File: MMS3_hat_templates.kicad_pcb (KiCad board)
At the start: 4 copper layers, 100 x 50 mm, 62 parts, among them J1 Chainbus in, J2 Chainbus Out, J3 Conn_01x04_Pin, J4 AMASS XT60 Male, J5 AMASS XT60 Female, J8 Conn_01x03_Pin, SW1 SW_DIP_x04, U2 M24C64, U3 SN74CB3Q3245PWR, U4 AMS1117, U5 LM2596HVS-ADJRG

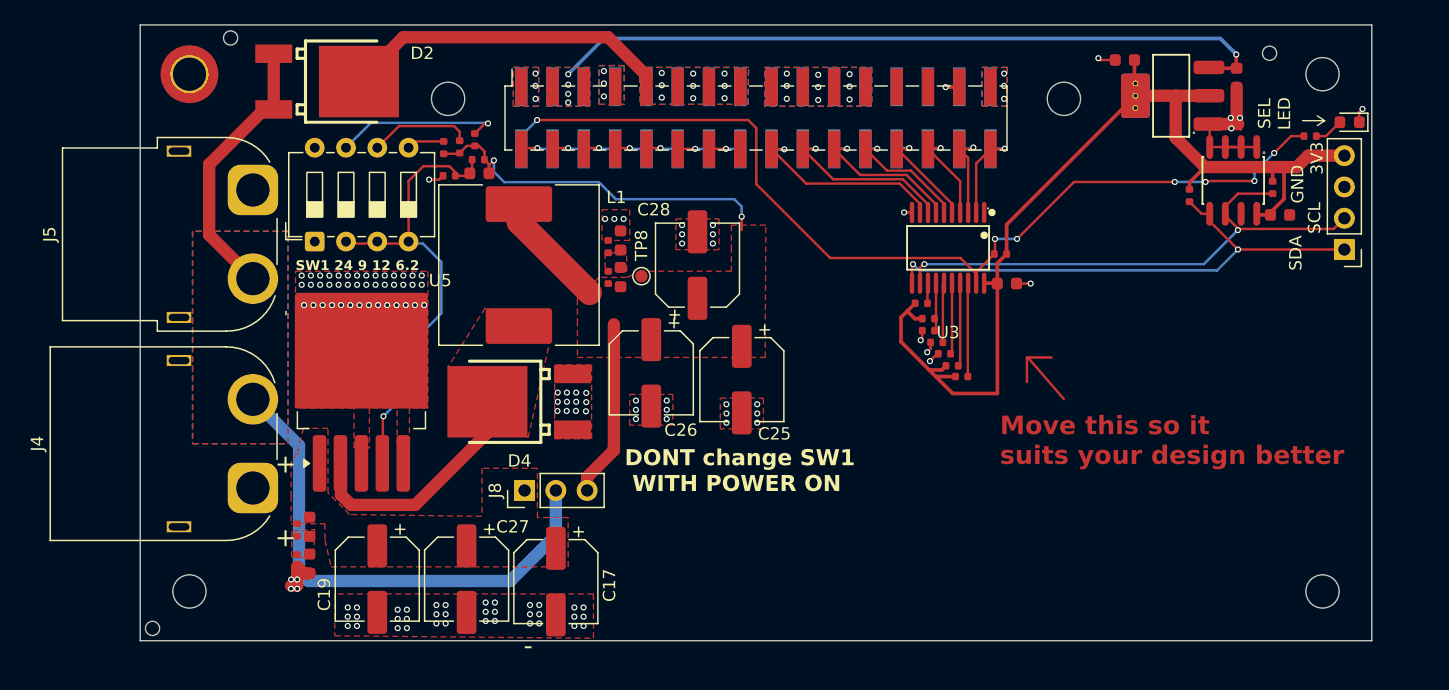
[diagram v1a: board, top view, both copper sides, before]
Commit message: added rounded corners
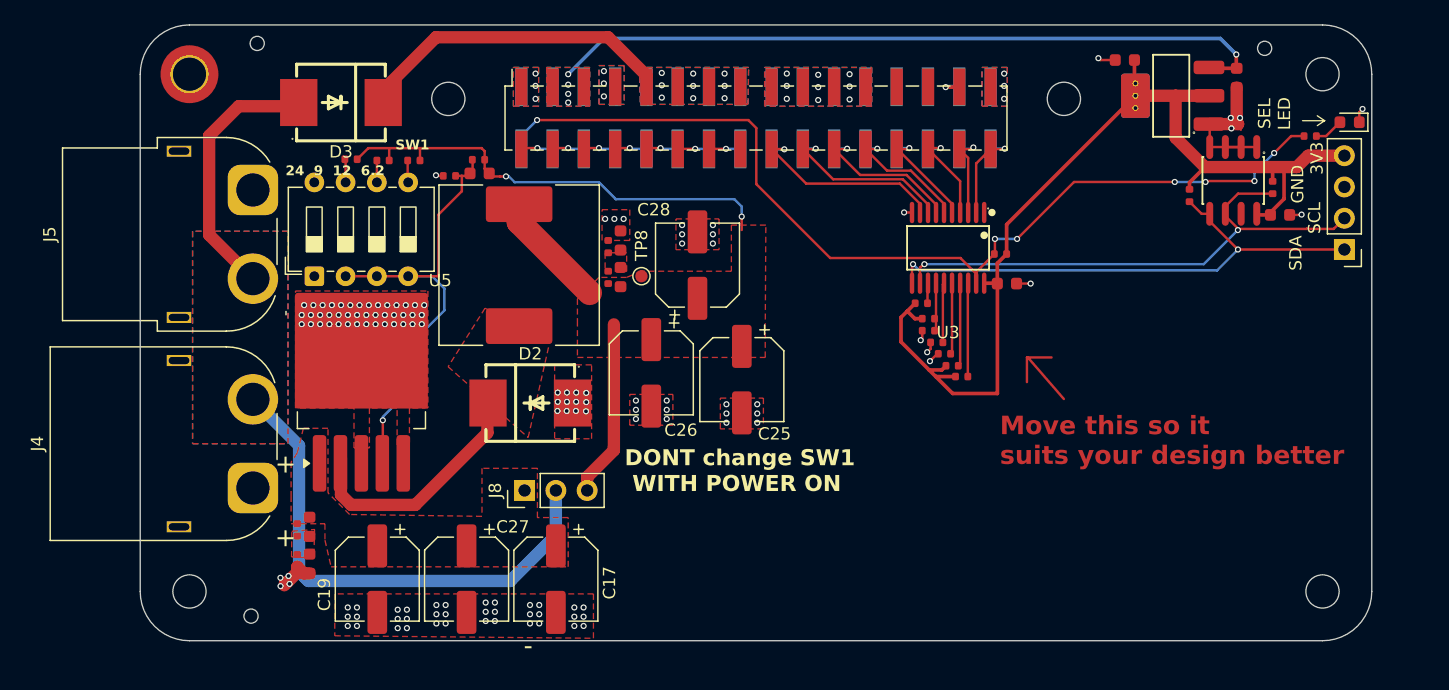
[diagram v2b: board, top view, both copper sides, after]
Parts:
- removed D4: MBRD10100CTTR, SMC_MBRD10100CTTR:TO-252-3_L6.5-W5.8-P4.58-TL
- removed PN1: ~, PCM_JLCPCB:Part_Num_JLCPCB
- added D3: SS510C, SS510C:SMC_L7.1-W6.2-LS8.1-RD, F.Cu at (94.3, 94.3)
- D2: value MBRD10100CTTR -> SS510C; footprint SMC_MBRD10100CTTR:TO-252-3_L6.5-W5.8-P4.58-TL -> SS510C:SMC_L7.1-W6.2-LS8.1-RD
- moved D2 31.4 mm to (109.7, 118.7)
- moved R14 10.2 mm to (95.1, 98.9), turned to 0 degrees
- moved H7 8.06 mm to (87.0, 136.0)
- moved R15 6.32 mm to (97.7, 99.0), turned to 0 degrees
- moved SW1 2.81 mm to (92.1, 108.4)
- moved R16 2.64 mm to (100.2, 99.0), turned to 0 degrees
- moved H9 2.21 mm to (87.5, 89.5)
- moved H8 0.57 mm to (169.3, 89.9)
- moved C17 0.20 mm to (111.8, 133.0)
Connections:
- D2 pad 1: Vin -> Net-(D2-K)
- D2 pad 2: BRD_VIN -> GND
- L1 pad 1: Net-(D4-K) -> Net-(D2-K)
- U5 pad 2: Net-(D4-K) -> Net-(D2-K)
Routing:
- net Net-(D4-K): track 21.4 -> 0.00 mm
- net Net-(D2-K): track 0.00 -> 21.4 mm
- net Net-(R14-Pad1): track 13.8 -> 1.90 mm, vias 1 -> 0
- net U_reg: track 55.0 -> 62.3 mm
- net Net-(R15-Pad1): track 8.34 -> 1.78 mm
- net GND: track 24.0 -> 25.7 mm, vias 144 -> 145
- net Net-(R16-Pad1): track 3.06 -> 1.80 mm
- net BRD_VIN: track 27.1 -> 25.9 mm
- added copper zone on F.Cu, net Net-(D2-K)
- removed copper zone on F.Cu, net Net-(D4-K)
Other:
- outline, holes or cut-outs redrawn
- board text added: "24 9 12 6.2"
- board text added: "Front and Back keepout zone for DIN rail mount"
- board text added: "SW1"
- board text removed: "SW1 24 9 12 6.2"
